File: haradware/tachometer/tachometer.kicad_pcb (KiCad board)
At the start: 2 copper layers, 48 x 72 mm, 16 parts, among them J1 Conn_01x03_Pin, J2 Conn_01x03_Pin, J3 Batt

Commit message: kicad編集
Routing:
- net (no net): vias 1 -> 0
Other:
- board text added: "WASA"

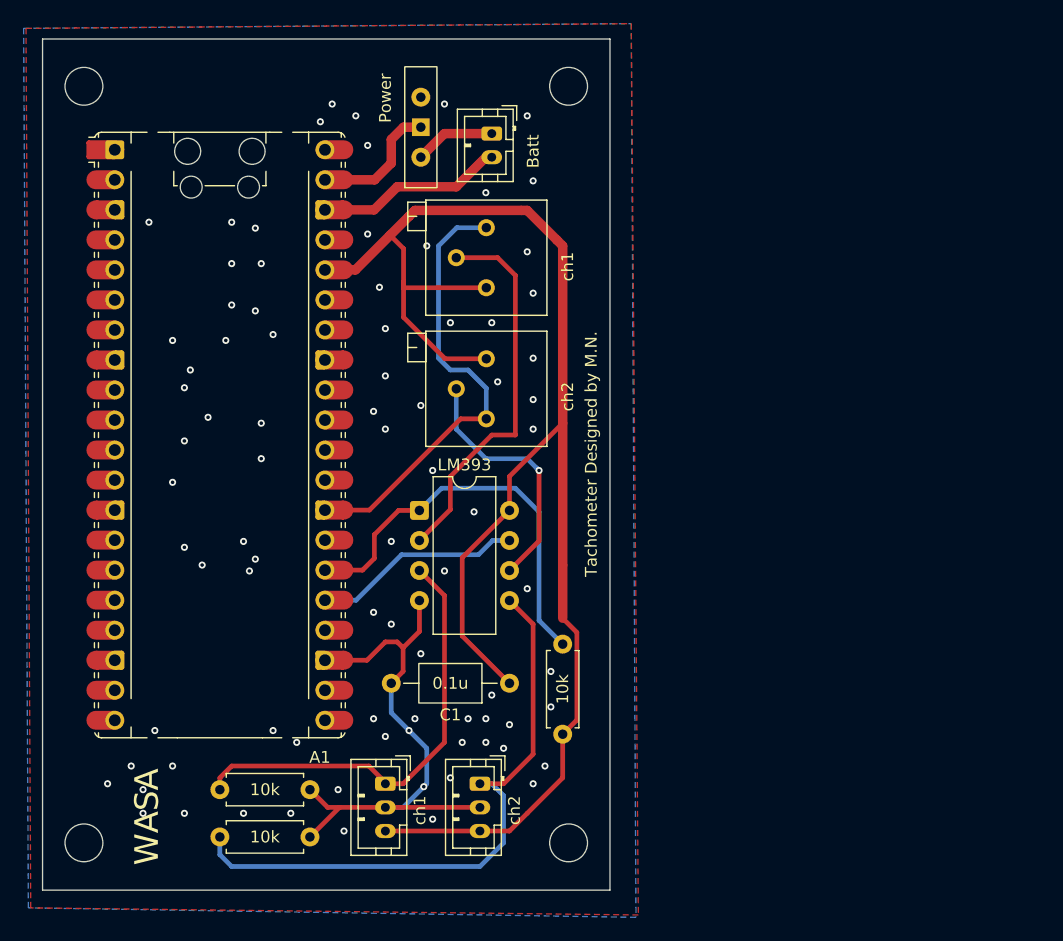
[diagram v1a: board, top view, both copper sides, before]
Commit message: 修正して再発注
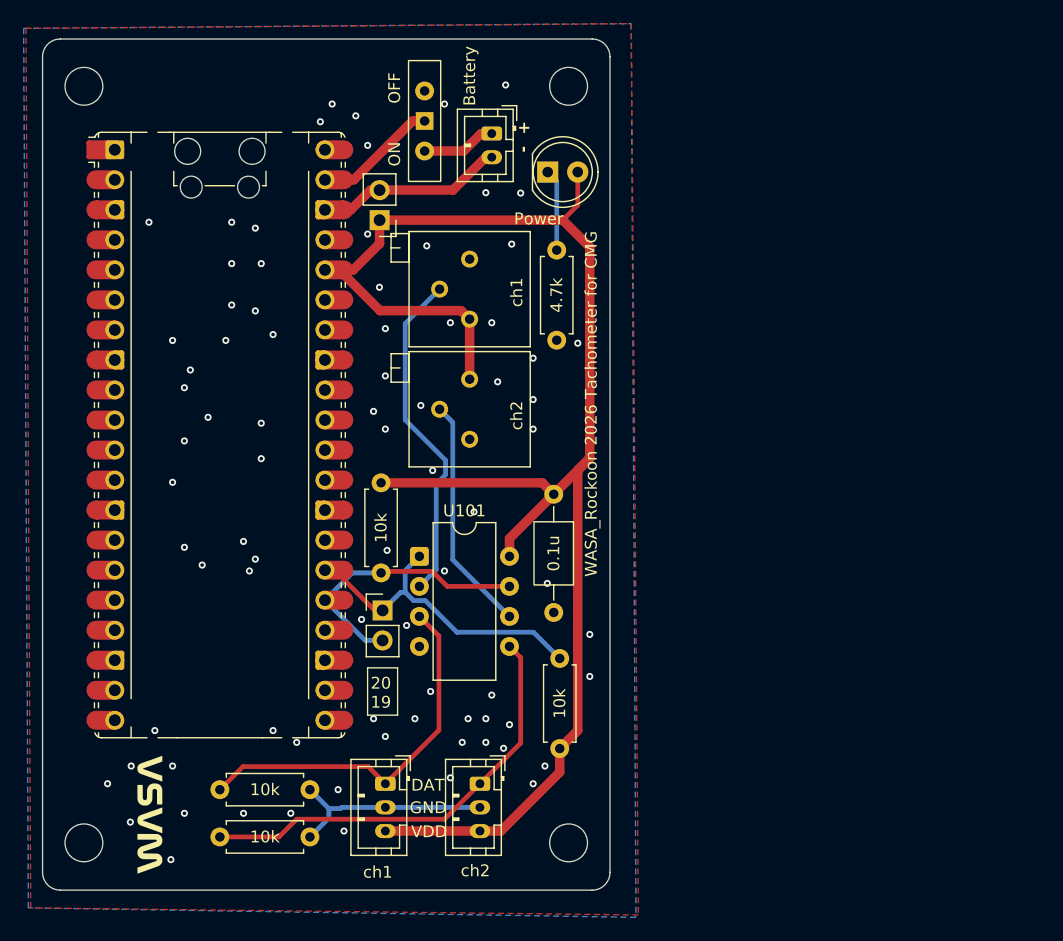
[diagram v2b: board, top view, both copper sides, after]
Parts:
- added D101: Power, LED_THT:LED_D5.0mm, F.Cu at (157.7, 63.8)
- added G***: LOGO, Library:wasa_10mm, F.Cu at (124.1, 118.1)
- added J101: OUT_EX, Connector_PinHeader_2.54mm:PinHeader_1x02_P2.54mm_Vertical, F.Cu at (143.8, 100.8)
- added J105: Power_EX, Connector_PinHeader_2.54mm:PinHeader_1x02_P2.54mm_Vertical, F.Cu at (143.5, 67.8)
- added R101: 10k, Resistor_THT:R_Axial_DIN0207_L6.3mm_D2.5mm_P7.62mm_Horizontal, F.Cu at (143.6, 90.0)
- added R105: 4.7k, Resistor_THT:R_Axial_DIN0207_L6.3mm_D2.5mm_P7.62mm_Horizontal, F.Cu at (158.5, 70.4)
- J102: renamed from J3; value Batt -> Battery
- J103: renamed from J2; value Conn_01x03_Pin -> ch2
- J104: renamed from J1; value Conn_01x03_Pin -> ch1
- U101: renamed from LM393; value LN393N -> LM393N
- moved C101 16.4 mm to (158.2, 91.0), turned to -90 degrees
- moved U101 3.89 mm to (146.9, 96.3)
- moved RV102 3.01 mm to (151.1, 71.1)
- moved RV101 2.23 mm to (151.1, 81.3)
- moved R102 1.24 mm to (158.8, 112.5)
- moved SW101 0.61 mm to (147.3, 59.4)
- renumbered A1 to A101, C1 to C101, R1 to R102, R2 to R103, R3 to R104, RV2 to RV101, RV1 to RV102, Power to SW101
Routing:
- net GND: track 99.8 -> 32.8 mm, vias 85 -> 82
- net Net-(J103-Pin_1): track 52.5 -> 37.3 mm
- net Net-(A101-GPIO20): track 34.2 -> 27.0 mm
- net Net-(D101-K): track 0.00 -> 6.92 mm
- net Net-(J104-Pin_1): track 37.9 -> 32.1 mm
- net Net-(A101-GPIO19): track 17.7 -> 23.4 mm
- net Net-(U101-IN1(-)): track 32.6 -> 28.7 mm
- net Net-(U101-IN2(-)): track 21.7 -> 20.0 mm, vias 1 -> 0
- net Net-(J102-Pin_1): track 6.33 -> 5.79 mm
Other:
- outline, holes or cut-outs redrawn
- board text added: "+ -"
- board text added: "20 19"
- board text added: "DAT"
- board text added: "GND"
- board text added: "OFF"
- board text added: "ON"
- board text added: "VDD"
- board text added: "WASA_Rockoon 2026 Tachometer for CMG"
- board text removed: "Tachometer Designed by M.N."
- board text removed: "WASA"
